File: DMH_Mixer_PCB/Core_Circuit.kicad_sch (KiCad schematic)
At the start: 0 parts

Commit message: PCB work in progress
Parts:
- added D1, D2: 1N4148, Diode_THT:D_DO-35_SOD27_P7.62mm_Horizontal, symbol Device:D
- added R1, R10, R2, R3, R4, R5, R6, R9: 100k, Resistor_THT:R_Axial_DIN0207_L6.3mm_D2.5mm_P7.62mm_Horizontal, symbol Device:R_US
- added R11: 27k, Resistor_THT:R_Axial_DIN0207_L6.3mm_D2.5mm_P7.62mm_Horizontal, symbol Device:R_US
- added R12, R7, R8: 1k, Resistor_THT:R_Axial_DIN0207_L6.3mm_D2.5mm_P7.62mm_Horizontal, symbol Device:R_US
- added RV1, RV2, RV3: 100k, Potentiometer_THT:Potentiometer_Alpha_RD901F-40-00D_Single_Vertical, symbol Device:R_Potentiometer_US
- added RV4: 20k, Potentiometer_THT:Potentiometer_Alpha_RD901F-40-00D_Single_Vertical, symbol Device:R_Potentiometer_US
- added U1: TL074, Package_DIP:DIP-14_W7.62mm_Socket, symbol Amplifier_Operational:TL074
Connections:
- new net: R10.2, R12.1, U1.8
- new net: R6.2, R7.1, R9.1, U1.7
- new net: D1.2 (A), D2.1 (K), R9.2, U1.10 (+)
- new net: R2.1, RV2.2
- new net: R1.2, R2.2, R3.2, R4.1, U1.2 (-)
- new net: D1.1 (K), D2.2 (A), RV4.3
- new net: R10.1, R11.2, U1.9 (-)
- new net: R1.1, RV1.2
- new net: R3.1, RV3.2
- new net: R4.2, R5.1, U1.1, U1.12 (+)
- new net: R8.1, U1.13 (-), U1.14
- new net: R5.2, R6.1, U1.6 (-)
- new net Clipped Output: R12.2
- new net GND: R11.1, RV1.1, RV2.1, RV3.1, RV4.1, RV4.2, U1.3 (+), U1.5 (+)
- new net Input 1: RV1.3
- new net Input 2: RV2.3
- new net Input 3: RV3.3
- new net Output +: R7.2
- new net Output -: R8.2
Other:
- note added: "Not necessary, just here in order to not leave idle one of the OpAmps in the chip."

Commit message: Component placing in progress
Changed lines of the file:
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@@
 	)
 	(hierarchical_label "Output +"
-		(shape input)
+		(shape output)
 		(at 139.7 78.74 0)
 		(fields_autoplaced yes)
@@
 	)
 	(hierarchical_label "Output -"
-		(shape input)
+		(shape output)
 		(at 139.7 38.1 0)
 		(fields_autoplaced yes)
@@
 	)
 	(hierarchical_label "Clipped Output"
-		(shape input)
+		(shape output)
 		(at 203.2 104.14 0)
 		(fields_autoplaced yes)

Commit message: Updated fps with their 3D models
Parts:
- RV1: footprint Potentiometer_THT:Potentiometer_Alpha_RD901F-40-00D_Single_Vertical -> SynthStuff:Potentiometer_Alpha_RD901F-40-00D_Single_Vertical; Function (none) -> Input 1 Gain
- RV2: footprint Potentiometer_THT:Potentiometer_Alpha_RD901F-40-00D_Single_Vertical -> SynthStuff:Potentiometer_Alpha_RD901F-40-00D_Single_Vertical; Function (none) -> Input 2 Gain
- RV3: footprint Potentiometer_THT:Potentiometer_Alpha_RD901F-40-00D_Single_Vertical -> SynthStuff:Potentiometer_Alpha_RD901F-40-00D_Single_Vertical; Function (none) -> Input 3 Gain
- RV4: footprint Potentiometer_THT:Potentiometer_Alpha_RD901F-40-00D_Single_Vertical -> SynthStuff:Potentiometer_Alpha_RD901F-40-00D_Single_Vertical; Function (none) -> Clipping Amount
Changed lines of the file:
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@@
 			)
 		)
-		(property "Footprint" "Potentiometer_THT:Potentiometer_Alpha_RD901F-40-00D_Single_Vertical"
+		(property "Footprint" "SynthStuff:Potentiometer_Alpha_RD901F-40-00D_Single_Vertical"
 			(at 139.7 120.65 0)
 			(effects
@@
 				)
 				(hide yes)
+			)
+		)
+		(property "Function" "Clipping Amount"
+			(at 124.968 120.65 0)
+			(effects
+				(font
+					(size 1.27 1.27)
+					(thickness 0.254)
+					(bold yes)
+					(italic yes)
+				)
 			)
 		)
@@
 			)
 		)
-		(property "Footprint" "Potentiometer_THT:Potentiometer_Alpha_RD901F-40-00D_Single_Vertical"
+		(property "Footprint" "SynthStuff:Potentiometer_Alpha_RD901F-40-00D_Single_Vertical"
 			(at 38.1 63.5 0)
 			(effects
@@
 			)
 		)
-		(property "Function" ""
-			(at 38.1 63.5 0)
-			(effects
-				(font
-					(size 1.27 1.27)
+		(property "Function" "Input 1 Gain"
+			(at 23.622 63.5 0)
+			(effects
+				(font
+					(size 1.27 1.27)
+					(thickness 0.254)
+					(bold yes)
+					(italic yes)
 				)
 			)
@@
 			)
 		)
-		(property "Footprint" "Potentiometer_THT:Potentiometer_Alpha_RD901F-40-00D_Single_Vertical"
+		(property "Footprint" "SynthStuff:Potentiometer_Alpha_RD901F-40-00D_Single_Vertical"
 			(at 38.1 88.9 0)
 			(effects
@@
 			)
 		)
-		(property "Function" ""
-			(at 38.1 88.9 0)
-			(effects
-				(font
-					(size 1.27 1.27)
+		(property "Function" "Input 2 Gain"
+			(at 23.876 88.9 0)
+			(effects
+				(font
+					(size 1.27 1.27)
+					(thickness 0.254)
+					(bold yes)
+					(italic yes)
 				)
 			)
@@
 			)
 		)
-		(property "Footprint" "Potentiometer_THT:Potentiometer_Alpha_RD901F-40-00D_Single_Vertical"
+		(property "Footprint" "SynthStuff:Potentiometer_Alpha_RD901F-40-00D_Single_Vertical"
 			(at 38.1 114.3 0)
 			(effects
@@
 			)
 		)
+		(property "Function" "Input 3 Gain"
+			(at 23.622 114.3 0)
+			(effects
+				(font
+					(size 1.27 1.27)
+					(thickness 0.254)
+					(bold yes)
+					(italic yes)
+				)
+			)
+		)

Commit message: Breadboarding ongoing
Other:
- note added: "10k to be tested"
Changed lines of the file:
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@@
+		)
+	)
+	(circle
+		(center 139.7 120.65)
+		(radius 6.35)
+		(stroke
+			(width 0)
+			(type default)
+		)
+		(fill
+			(type none)
 		)
 	)
@@
 		(effects
 			(font
+				(size 1.27 1.27)
+			)
+		)
+	)
+	(text "10k to be tested"
+		(exclude_from_sim no)
+		(at 148.844 116.84 0)
+		(effects
+			(font

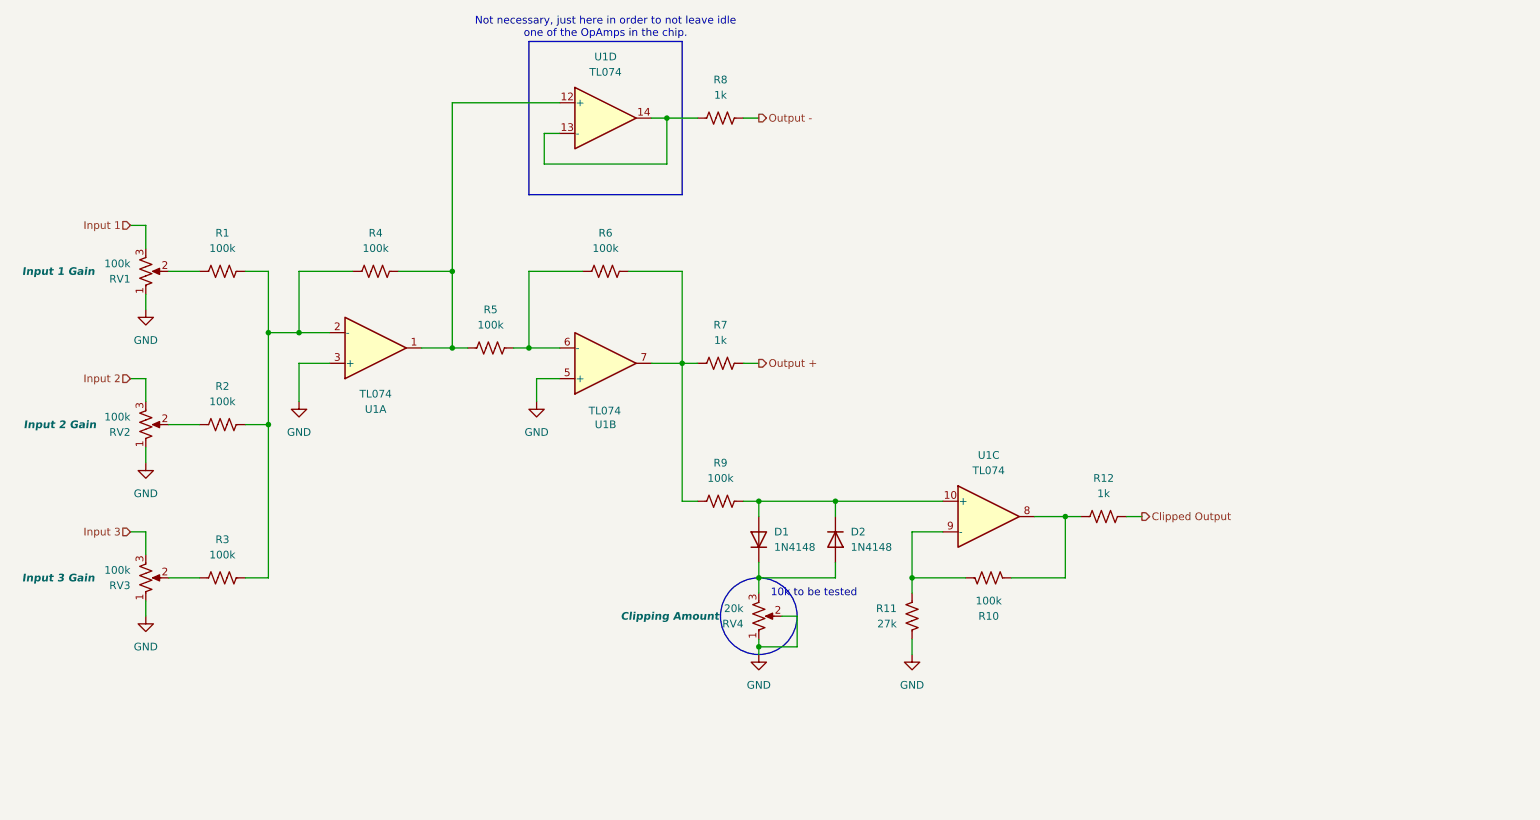
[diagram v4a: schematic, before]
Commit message: Added 4th channel to schematic
... and replaced Inverted Output with Clipped Output
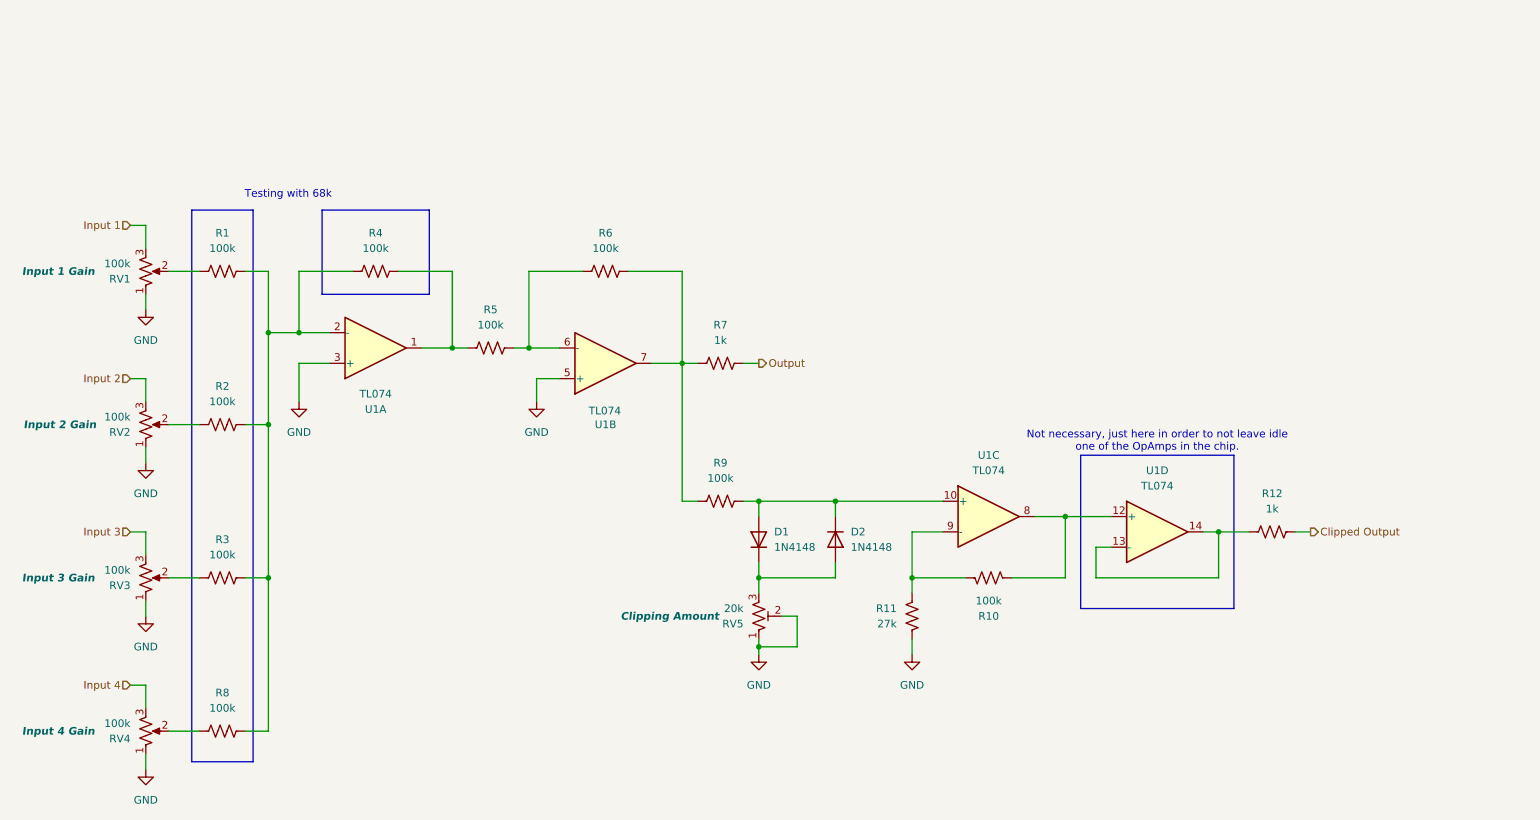
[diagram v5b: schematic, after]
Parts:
- added RV4: 100k, SynthStuff:Potentiometer_Alpha_RD901F-40-00D_Single_Vertical, symbol Device:R_Potentiometer_US
- R8: value 1k -> 100k
- RV5: renamed from RV4; symbol Device:R_Potentiometer_US -> Device:R_Potentiometer_Trim_US
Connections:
- net Output - is gone; now on an unnamed net: R8.2
- net GND: now also RV4.1
- net at R10.2, U1.8: now also U1.12 (+); no longer R12.1
- net at R4.2, R5.1, U1.1: no longer U1.12 (+)
- net at U1.13 (-), U1.14: now also R12.1; no longer R8.1
- net Output + renamed Output
- new net: R8.1, RV4.2
- new net Input 4: RV4.3
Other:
- note added: "Testing with 68k"
- note removed: "10k to be tested"
- moved on the sheet: R12, U1D

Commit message: PCB redesign in progress
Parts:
- RV5: footprint SynthStuff:Potentiometer_Alpha_RD901F-40-00D_Single_Vertical -> Potentiometer_THT:Potentiometer_Bourns_3296W_Vertical
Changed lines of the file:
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@@
 			)
 		)
-		(property "Footprint" "SynthStuff:Potentiometer_Alpha_RD901F-40-00D_Single_Vertical"
+		(property "Footprint" "Potentiometer_THT:Potentiometer_Bourns_3296W_Vertical"
 			(at 139.7 120.65 0)
 			(effects

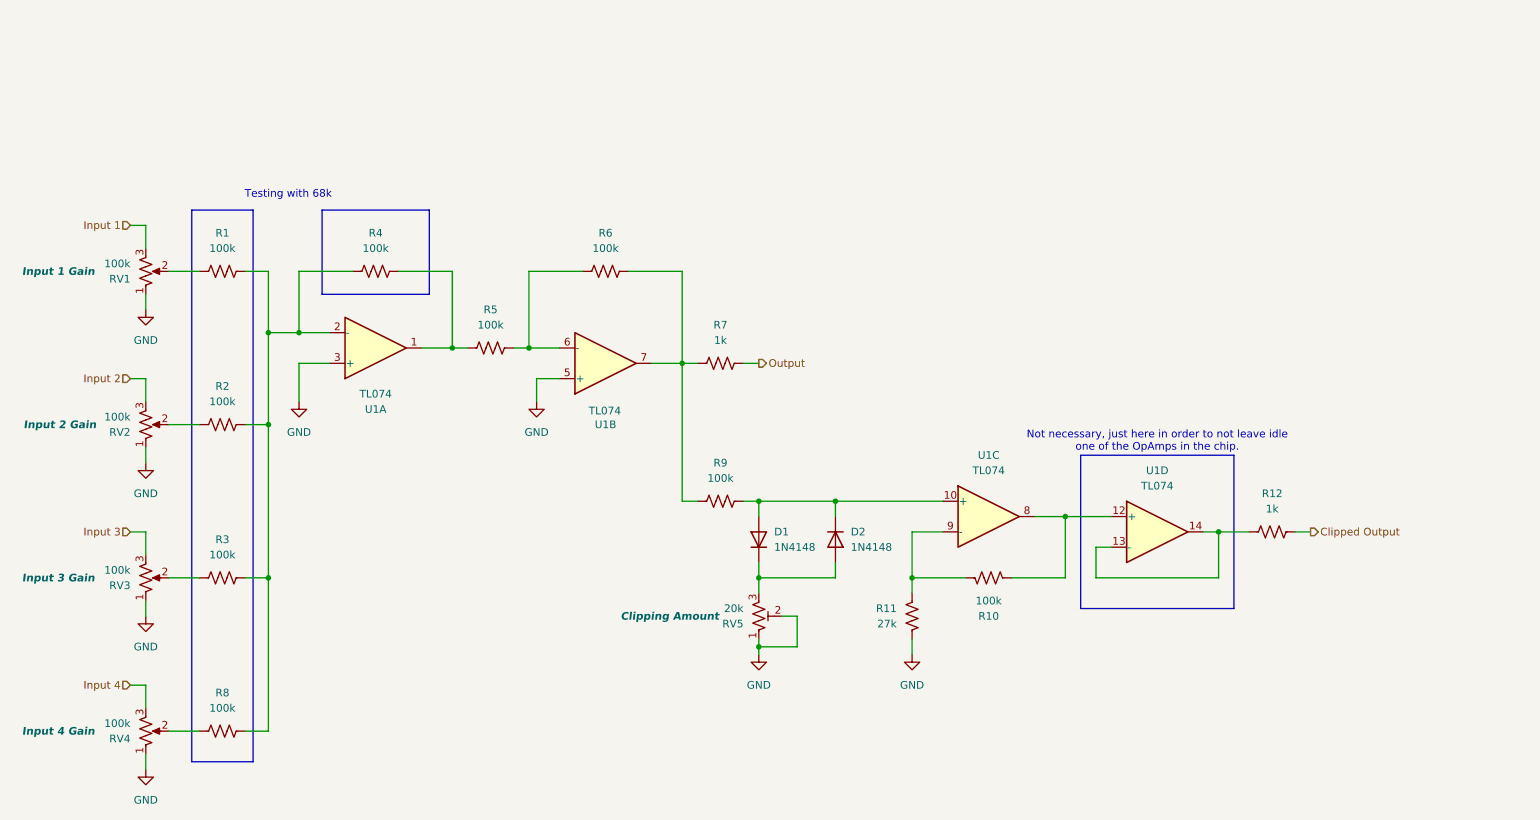
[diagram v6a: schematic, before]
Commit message: Added switches to schematic
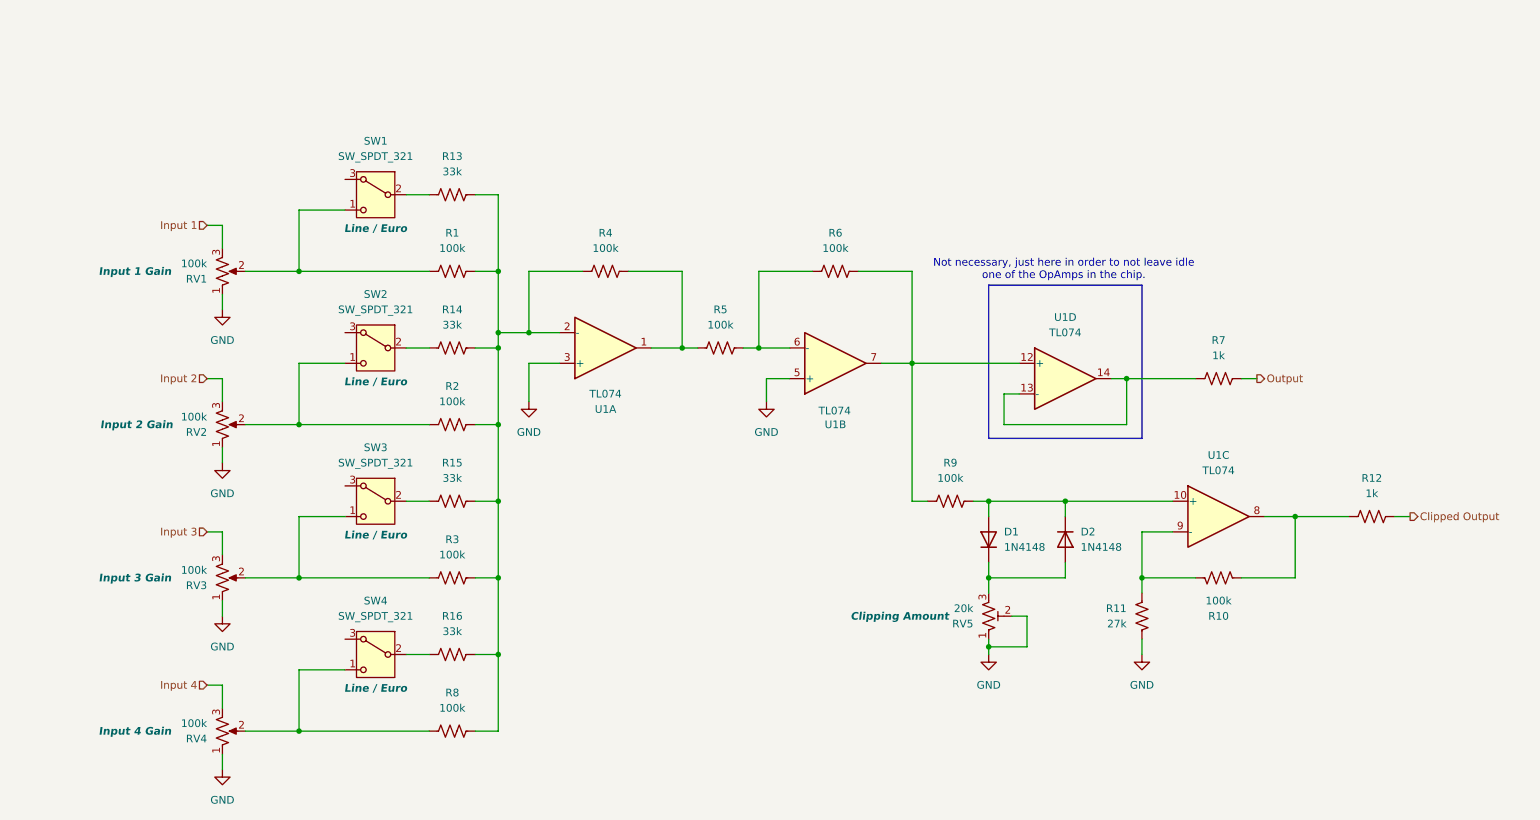
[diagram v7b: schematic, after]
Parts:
- added R13, R14, R15, R16: 33k, Resistor_THT:R_Axial_DIN0207_L6.3mm_D2.5mm_P7.62mm_Horizontal, symbol Device:R_US
- added SW1, SW2, SW3, SW4: SW_SPDT_321, SynthStuff:Toggle_Switch_THT, symbol Switch:SW_SPDT_321
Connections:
- net at U1.13 (-), U1.14: now also R7.1; no longer R12.1
- net at R6.2, R9.1, U1.7: now also U1.12 (+); no longer R7.1
- net at R2.1, RV2.2: now also SW2.1 (C)
- net at R1.2, R2.2, R3.2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: now also R13.2, R14.2, R15.2, R16.2
- net at R10.2, U1.8: now also R12.1; no longer U1.12 (+)
- net at R8.1, RV4.2: now also SW4.1 (C)
- net at R1.1, RV1.2: now also SW1.1 (C)
- net at R3.1, RV3.2: now also SW3.1 (C)
- new net: R14.1, SW2.2 (B)
- new net: R15.1, SW3.2 (B)
- new net: R13.1, SW1.2 (B)
- new net: R16.1, SW4.2 (B)
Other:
- note removed: "Testing with 68k"
- moved on the sheet: D1, D2, R1, R10, R11, R12, R2, R3, R4, R5, R6, R7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

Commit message: Component placement ongoing
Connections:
- no-connect marks 0 -> 4
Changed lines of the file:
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@@
 		(color 0 0 0 0)
+	)
+	(no_connect
+		(at 71.12 124.46)
+	)
+	(no_connect
+		(at 71.12 48.26)
+	)
+	(no_connect
+		(at 71.12 73.66)
+	)
+	(no_connect
+		(at 71.12 99.06)
 	)
 	(wire
